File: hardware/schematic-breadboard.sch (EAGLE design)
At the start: 41 parts, among them IC1 LM7805C, IC3 NTE1904, Q1 2N3819, X1 SMA-142-0701-801/806

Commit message: Add a script which parses the massive log files and can pare them down to smaller data sets. Also add a sample data run [yes, it was taken while standing still, but is within reason]
Added connections for I2C and temperature sensor to breadboard schematic. Should fix #11 unless there is more to be added.
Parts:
- added JP1: TMP102, SparkFun-Connectors:M04PTH
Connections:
- net N$1 renamed PB6
- net N$10 renamed +9V
- net N$11 renamed EN
- net N$14 renamed RF
- net N$18 renamed PC4
- net N$24 renamed TX-B
- net N$25 renamed RX-B
- net N$29 renamed TX
- net N$30 renamed RX
- net N$5 renamed RFGND
- net N$7 renamed RFOUT
- net N$9 renamed PD1
- removed net N$16: C10.+, IC3.OUT
- removed net N$21: C12.+, IC1.OUT
- new net SCL: JP1.4, TIVA_1.17
- new net SDA: JP1.3, TIVA_1.19
- net +3V3: now also C10.+, IC3.OUT, JP1.1
- net +5V: now also C12.+, IC1.OUT
- net GNDA: now also JP1.2
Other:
- note removed: "PB6"
- note removed: "PC4"
- note removed: "PD1"
- note removed: "RX"
- note removed: "RX-B"
- note removed: "TX"
- note removed: "TX-B"

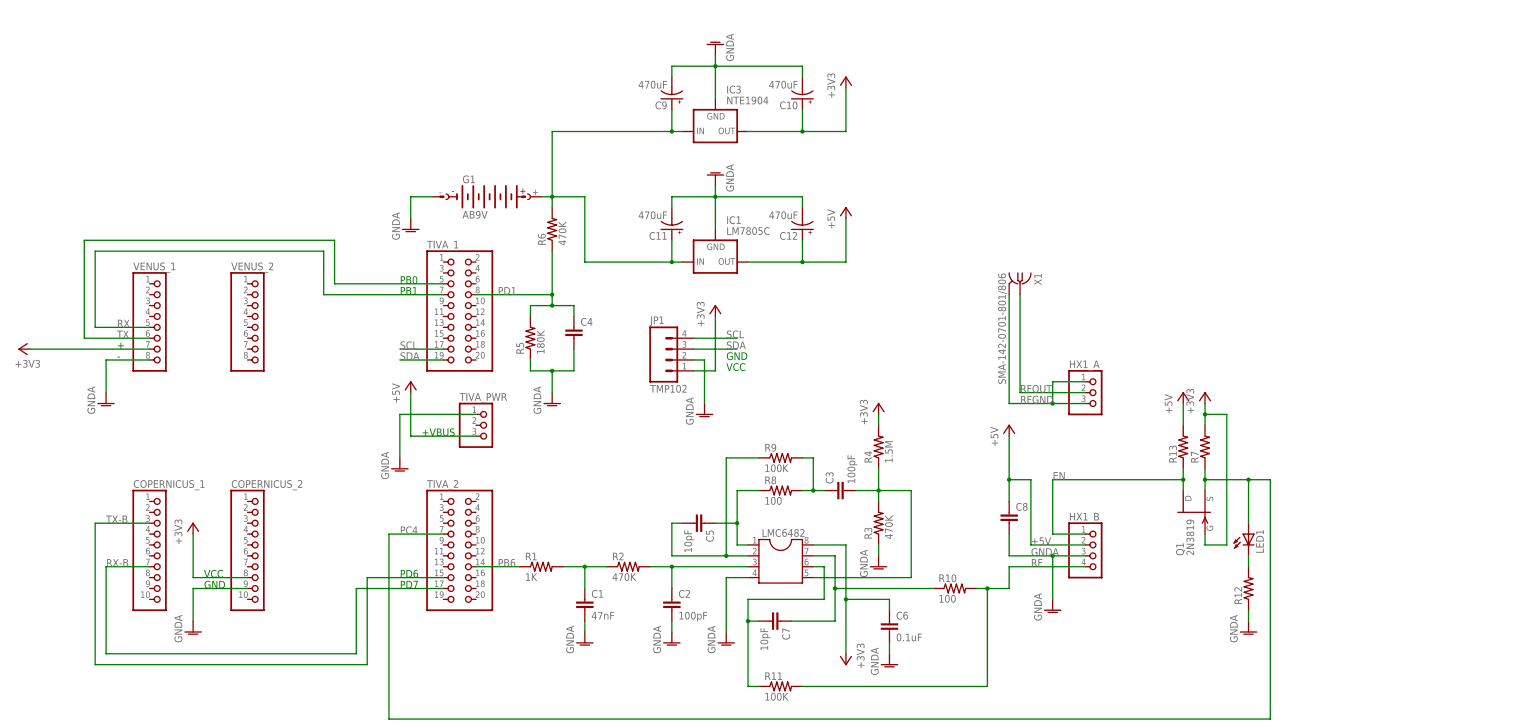
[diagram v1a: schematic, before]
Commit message: changed breadboard to reflect PCB design
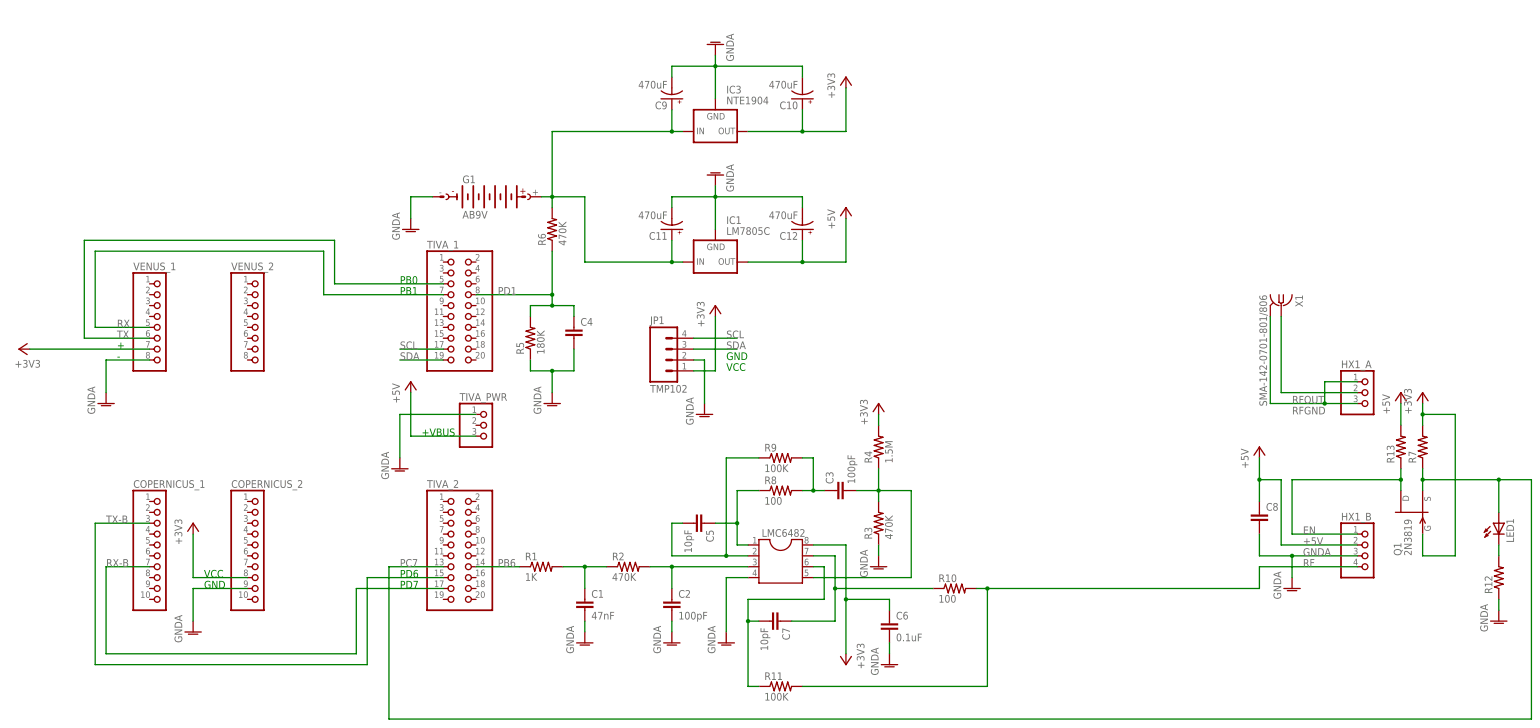
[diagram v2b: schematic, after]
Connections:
- removed net PC4: LED1.A, Q1.S, R7.1, TIVA_2.7
- new net PC7: LED1.A, Q1.S, R7.1, TIVA_2.13
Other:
- moved on the sheet: C8, HX1_A, HX1_B, LED1, Q1, R12, R13, R7, X1

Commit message: - added specs to repository - fixed some warnings - added manual input gps fix mode to supported list and fixed unit tests - added raspberry pi connection to breadboard schematic
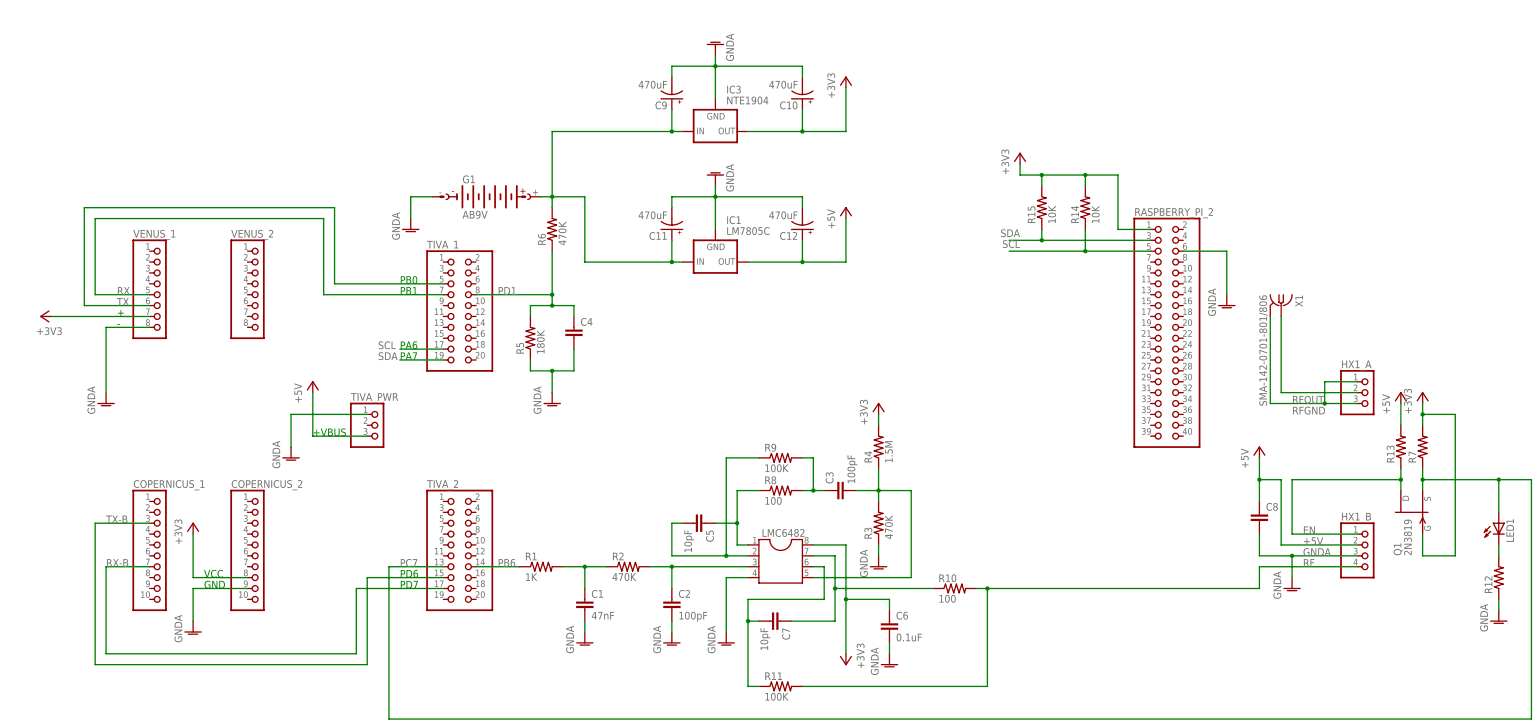
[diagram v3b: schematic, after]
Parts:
- removed JP1: TMP102, SparkFun-Connectors:M04PTH
- added R14, R15: 10K, resistor:R-US_0204/2V
- added RASPBERRY_PI_2: (no value), pinhead:PINHD-2X20
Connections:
- net +3V3: now also R14.2, R15.2, RASPBERRY_PI_2.1; no longer JP1.1
- net GNDA: now also RASPBERRY_PI_2.6; no longer JP1.2
- net SCL: now also R14.1, RASPBERRY_PI_2.5; no longer JP1.4
- net SDA: now also R15.1, RASPBERRY_PI_2.3; no longer JP1.3
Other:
- note added: "PA6"
- note added: "PA7"
- moved on the sheet: TIVA_PWR, VENUS_1, VENUS_2

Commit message: added accelerometer schematics (for breadboard)
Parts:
- added ADXL345_SPARKFUN: (no value), pinhead:PINHD-1X8
- added R16: 10K, resistor:R-US_0204/2V
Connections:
- new net N$9: ADXL345_SPARKFUN.6, R16.1
- new net SDL: ADXL345_SPARKFUN.1
- net +3V3: now also ADXL345_SPARKFUN.7, R16.2
- net GNDA: now also ADXL345_SPARKFUN.3, ADXL345_SPARKFUN.8
- net SDA: now also ADXL345_SPARKFUN.2
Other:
- note added: "CS"
- note added: "SCL"
- note added: "SD0"
- note added: "SDA"
- note added: "Temperature sensor is attached as is. SDA to SDA, SCL to SCL, etc."
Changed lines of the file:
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@@
 <part name="R14" library="resistor" deviceset="R-US_" device="0204/2V" value="10K"/>
 <part name="R15" library="resistor" deviceset="R-US_" device="0204/2V" value="10K"/>
+<part name="ADXL345_SPARKFUN" library="pinhead" deviceset="PINHD-1X8" device=""/>
+<part name="GND15" library="supply1" deviceset="GNDA" device=""/>
+<part name="+3V7" library="supply1" deviceset="+3V3" device=""/>
+<part name="R16" library="resistor" deviceset="R-US_" device="0204/2V" value="10K"/>
 </parts>
 <sheets>
@@
 <text x="-10.16" y="63.5" size="1.778" layer="91">PA6</text>
 <text x="-10.16" y="60.96" size="1.778" layer="91">PA7</text>
+<text x="154.94" y="83.82" size="1.778" layer="91" rot="R180">Temperature sensor is attached as is.
+SDA to SDA, SCL to SCL, etc.</text>
+<text x="160.02" y="137.16" size="1.778" layer="91">SCL</text>
+<text x="160.02" y="134.62" size="1.778" layer="91">SDA</text>
+<text x="160.02" y="132.08" size="1.778" layer="91">SD0</text>
+<text x="160.02" y="124.46" size="1.778" layer="91">CS</text>
+<text x="160.02" y="121.92" size="1.778" layer="91">VCC</text>
+<text x="160.02" y="119.38" size="1.778" layer="91">GND</text>
 </plain>
 <instances>
@@
 <instance part="R14" gate="G$1" x="149.86" y="96.52" rot="R90"/>
 <instance part="R15" gate="G$1" x="139.7" y="96.52" rot="R90"/>
+<instance part="ADXL345_SPARKFUN" gate="A" x="172.72" y="127"/>
+<instance part="GND15" gate="1" x="157.48" y="114.3"/>
+<instance part="+3V7" gate="G$1" x="139.7" y="132.08"/>
+<instance part="R16" gate="G$1" x="147.32" y="124.46" rot="R180"/>
 </instances>
 <busses>
@@
 <pinref part="GND16" gate="1" pin="GNDA"/>
 <wire x1="182.88" y1="86.36" x2="182.88" y2="76.2" width="0.1524" layer="91"/>
+</segment>
+<segment>
+<pinref part="GND15" gate="1" pin="GNDA"/>
+<wire x1="157.48" y1="116.84" x2="157.48" y2="119.38" width="0.1524" layer="91"/>
+<pinref part="ADXL345_SPARKFUN" gate="A" pin="8"/>
+<wire x1="170.18" y1="119.38" x2="157.48" y2="119.38" width="0.1524" layer="91"/>
+<junction x="157.48" y="119.38"/>
+<pinref part="ADXL345_SPARKFUN" gate="A" pin="3"/>
+<wire x1="170.18" y1="132.08" x2="157.48" y2="132.08" width="0.1524" layer="91"/>
+<wire x1="157.48" y1="132.08" x2="157.48" y2="119.38" width="0.1524" layer="91"/>
 </segment>
 </net>
@@
 <pinref part="R14" gate="G$1" pin="2"/>
 <wire x1="149.86" y1="101.6" x2="149.86" y2="104.14" width="0.1524" layer="91"/>
+</segment>
+<segment>
+<pinref part="+3V7" gate="G$1" pin="+3V3"/>
+<wire x1="139.7" y1="129.54" x2="139.7" y2="124.46" width="0.1524" layer="91"/>
+<pinref part="R16" gate="G$1" pin="2"/>
+<wire x1="139.7" y1="124.46" x2="142.24" y2="124.46" width="0.1524" layer="91"/>
+<junction x="139.7" y="124.46"/>
+<wire x1="139.7" y1="124.46" x2="139.7" y2="121.92" width="0.1524" layer="91"/>
+<pinref part="ADXL345_SPARKFUN" gate="A" pin="7"/>
+<wire x1="139.7" y1="121.92" x2="170.18" y2="121.92" width="0.1524" layer="91"/>
 </segment>
 </net>
@@
 <wire x1="139.7" y1="91.44" x2="139.7" y2="88.9" width="0.1524" layer="91"/>
 </segment>
-</net>
+<segment>
+<pinref part="ADXL345_SPARKFUN" gate="A" pin="2"/>
+<wire x1="170.18" y1="134.62" x2="160.02" y2="134.62" width="0.1524" layer="91"/>
+</segment>
+</net>
+<net name="SDL" class="0">
+<segment>
+<pinref part="ADXL345_SPARKFUN" gate="A" pin="1"/>
+<wire x1="170.18" y1="137.16" x2="160.02" y2="137.16" width="0.1524" layer="91"/>
+</segment>
+</net>
+<net name="N$9" class="0">
+<segment>
+<pinref part="ADXL345_SPARKFUN" gate="A" pin="6"/>
+<wire x1="170.18" y1="124.46" x2="152.4" y2="124.46" width="0.1524" layer="91"/>
+<pinref part="R16" gate="G$1" pin="1"/>
+</segment>
+</net>
